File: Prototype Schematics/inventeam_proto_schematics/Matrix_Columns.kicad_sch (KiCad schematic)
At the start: 37 parts, among them J1 Conn_02x20_Top_Bottom, J2 Conn_01x03, J3 Screw_Terminal_01x02, U1 MCP23S17_SP, U2 TMUX1208PW, U3 MCP23S17_SP, U4 TMUX1208PW, U5 MCP1525-TO, U6 OPA2333xxD

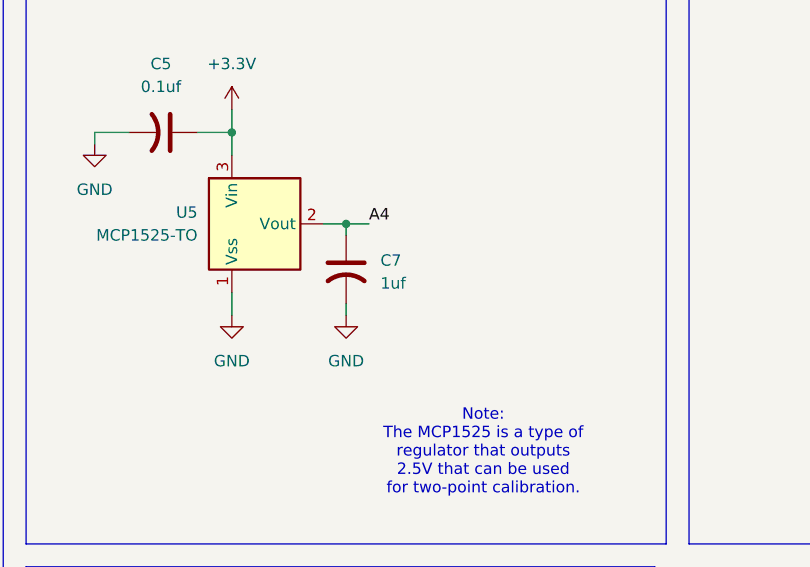
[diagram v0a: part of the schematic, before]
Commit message: Change 1uf to 10uf
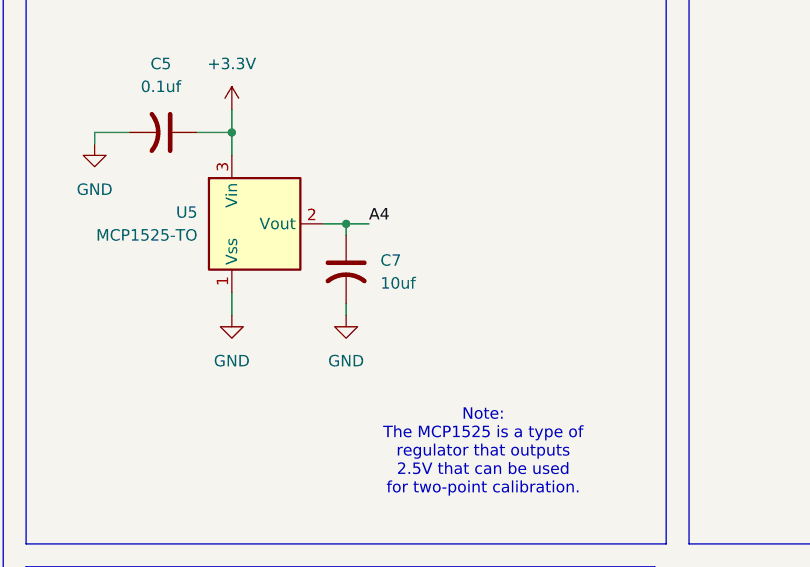
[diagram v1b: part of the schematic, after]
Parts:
- C7: value 1uf -> 10uf
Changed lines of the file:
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@@
 			)
 		)
-		(property "Value" "1uf"
+		(property "Value" "10uf"
 			(at 228.6 180.5939 0)
 			(effects

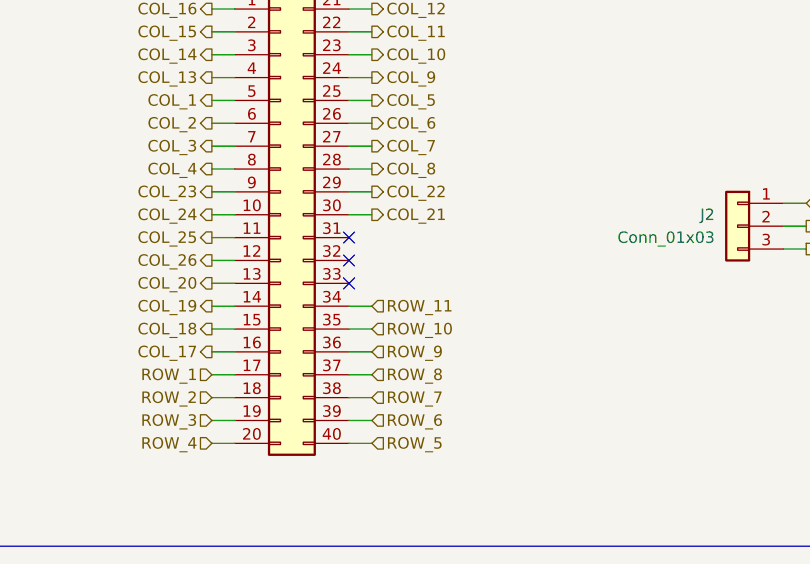
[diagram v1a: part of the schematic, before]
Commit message: Minor fix on row header
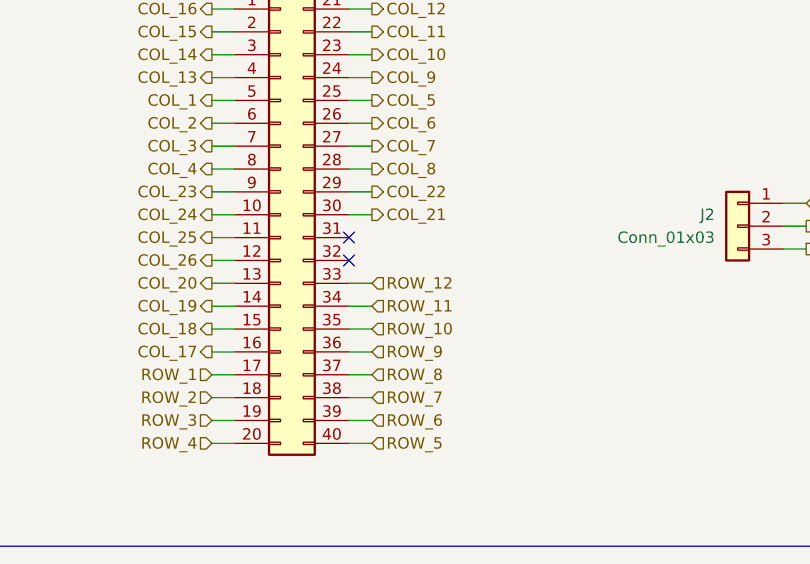
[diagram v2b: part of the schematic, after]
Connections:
- net ROW_12: now also J1.33 (Pin_33)
- no-connect marks 26 -> 25
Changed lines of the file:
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@@
 	)
 	(no_connect
-		(at 83.82 309.88)
-	)
-	(no_connect
 		(at 323.85 147.32)
 	)
@@
 	(wire
 		(pts
+			(xy 83.82 309.88) (xy 86.36 309.88)
+		)
+		(stroke
+			(width 0)
+			(type default)
+		)
+	)
+	(wire
+		(pts
 			(xy 67.31 185.42) (xy 67.31 207.01)
 		)
@@
 		(effects
 			(font
+				(size 1.27 1.27)
+			)
+			(justify left)
+		)
+	)
+	(hierarchical_label "ROW_12"
+		(shape input)
+		(at 86.36 309.88 0)
+		(effects
+			(font

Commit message: Schematic V16
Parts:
- added C23, C24: 1nf, symbol Device:C_US
- added R341, R343: 220, symbol Device:R_US
- added R342, R344: 1M, symbol Device:R_US
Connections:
- net AMP_NON_IN_1: now also C23.1, R341.2; no longer U2.8 (D)
- net AMP_NON_IN_2: now also C24.1, R343.2; no longer U4.8 (D)
- net GND: now also C23.2, C24.2, R342.2, R344.2
- new net: R341.1, R342.1, U2.8 (D)
- new net: R343.1, R344.1, U4.8 (D)
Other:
- moved on the sheet: A1, BT1, C1, C10, C11, C3, C5, C6, C7, C8, C9, F1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
